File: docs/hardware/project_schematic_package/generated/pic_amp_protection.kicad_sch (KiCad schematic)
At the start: 0 parts

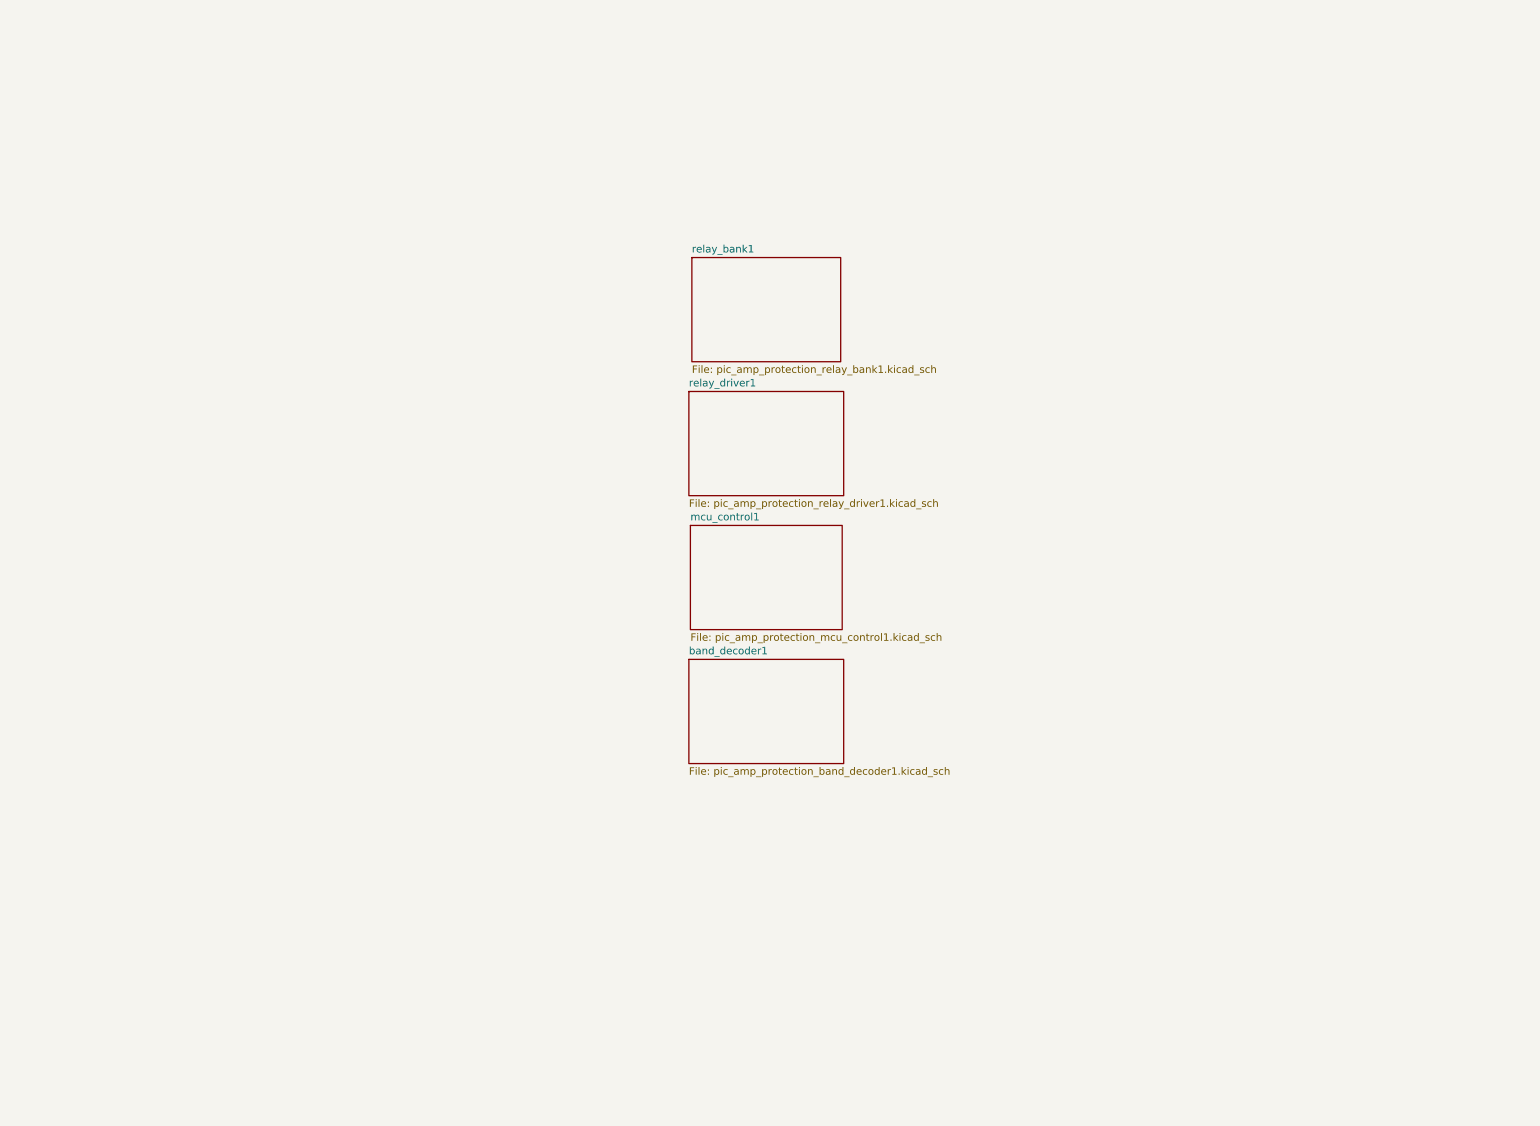
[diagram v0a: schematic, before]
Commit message: Create validated MCP schematic foundation
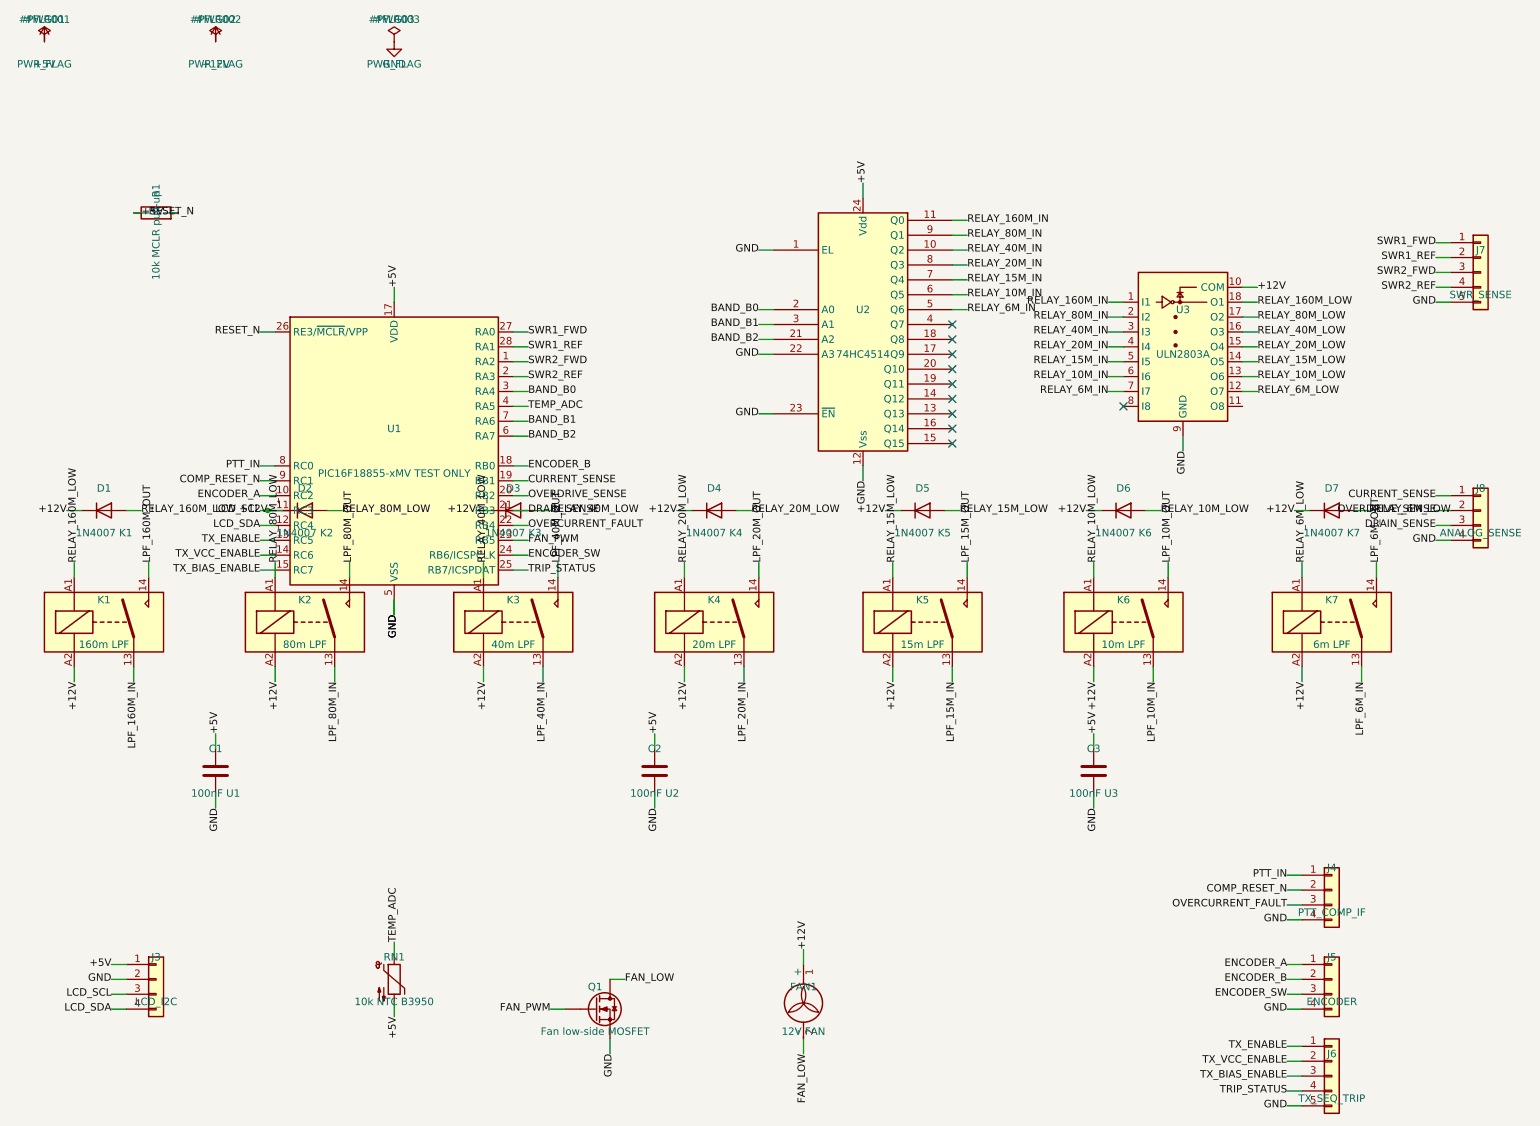
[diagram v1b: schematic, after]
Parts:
- added C1: 100nF U1, symbol Device:C
- added C2: 100nF U2, symbol Device:C
- added C3: 100nF U3, symbol Device:C
- added D1: 1N4007 K1, symbol Device:D
- added D2: 1N4007 K2, symbol Device:D
- added D3: 1N4007 K3, symbol Device:D
- added D4: 1N4007 K4, symbol Device:D
- added D5: 1N4007 K5, symbol Device:D
- added D6: 1N4007 K6, symbol Device:D
- added D7: 1N4007 K7, symbol Device:D
- added FAN1: 12V FAN, symbol Motor:Fan
- added J3: LCD_I2C, symbol Connector_Generic:Conn_01x04
- added J4: PTT_COMP_IF, symbol Connector_Generic:Conn_01x04
- added J5: ENCODER, symbol Connector_Generic:Conn_01x04
- added J6: TX_SEQ_TRIP, symbol Connector_Generic:Conn_01x05
- added J7: SWR_SENSE, symbol Connector_Generic:Conn_01x05
- added J8: ANALOG_SENSE, symbol Connector_Generic:Conn_01x04
- added K1: 160m LPF, symbol Relay:Relay_SPST-NO
- added K2: 80m LPF, symbol Relay:Relay_SPST-NO
- added K3: 40m LPF, symbol Relay:Relay_SPST-NO
- added K4: 20m LPF, symbol Relay:Relay_SPST-NO
- added K5: 15m LPF, symbol Relay:Relay_SPST-NO
- added K6: 10m LPF, symbol Relay:Relay_SPST-NO
- added K7: 6m LPF, symbol Relay:Relay_SPST-NO
- added Q1: Fan low-side MOSFET, symbol Device:Q_NMOS
- added R1: 10k MCLR pull-up, symbol Device:R
- added RN1: 10k NTC B3950, symbol Device:Thermistor_NTC
- added U1: PIC16F18855-xMV TEST ONLY, symbol MCU_Microchip_PIC16:PIC16F18855-xMV
- added U2: 74HC4514, symbol 4xxx_IEEE:4514
- added U3: ULN2803A, symbol Transistor_Array:ULN2803A
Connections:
- new net +12V: D1.1 (K), D2.1 (K), D3.1 (K), D4.1 (K), D5.1 (K), D6.1 (K), D7.1 (K), FAN1.1 (+), J3.3 (Pin_3), K1.A2, K2.A2, K3.A2, K4.A2, K5.A2, K6.A2, K7.A2, U1.11 (RC3), U3.10 (COM)
- new net +5V: C1.1, C2.1, C3.1, J3.1 (Pin_1), R1.2, RN1.2, U1.17 (VDD), U2.24 (Vdd)
- new net BAND_B0: U1.3 (RA4), U2.2 (A0)
- new net BAND_B1: U1.7 (RA6), U2.3 (A1)
- new net BAND_B2: U1.6 (RA7), U2.21 (A2)
- new net COMP_RESET_N: J4.2 (Pin_2), U1.9 (RC1)
- new net CURRENT_SENSE: J8.1 (Pin_1), U1.19 (RB1)
- new net DRAIN_SENSE: J8.3 (Pin_3), U1.21 (RB3)
- new net ENCODER_A: J5.1 (Pin_1), U1.10 (RC2)
- new net ENCODER_B: J5.2 (Pin_2), U1.18 (RB0)
- new net ENCODER_SW: J5.3 (Pin_3), U1.24 (RB6/ICSPCLK)
- new net FAN_LOW: FAN1.2 (-), Q1.D
- new net FAN_PWM: Q1.G, U1.23 (RB5)
- new net GND: C1.2, C2.2, C3.2, J3.2 (Pin_2), J4.4 (Pin_4), J5.4 (Pin_4), J6.5 (Pin_5), J7.5 (Pin_5), J8.4 (Pin_4), Q1.S, U1.16 (VSS), U1.29 (VSS), U1.5 (VSS), U2.1 (EL), U2.12 (Vss), U2.22 (A3), U2.23 (~{EN}), U3.9 (GND)
- new net LCD_SDA: J3.4 (Pin_4), U1.12 (RC4)
- new net LPF_10M_IN: K6.13
- new net LPF_10M_OUT: K6.14
- new net LPF_15M_IN: K5.13
- new net LPF_15M_OUT: K5.14
- new net LPF_160M_IN: K1.13
- new net LPF_160M_OUT: K1.14
- new net LPF_20M_IN: K4.13
- new net LPF_20M_OUT: K4.14
- new net LPF_40M_IN: K3.13
- new net LPF_40M_OUT: K3.14
- new net LPF_6M_IN: K7.13
- new net LPF_6M_OUT: K7.14
- new net LPF_80M_IN: K2.13
- new net LPF_80M_OUT: K2.14
- new net OVERCURRENT_FAULT: J4.3 (Pin_3), U1.22 (RB4)
- new net OVERDRIVE_SENSE: J8.2 (Pin_2), U1.20 (RB2)
- new net PTT_IN: J4.1 (Pin_1), U1.8 (RC0)
- new net RELAY_10M_IN: U2.6 (Q5), U3.6 (I6)
- new net RELAY_10M_LOW: D6.2 (A), K6.A1, U3.13 (O6)
- new net RELAY_15M_IN: U2.7 (Q4), U3.5 (I5)
- new net RELAY_15M_LOW: D5.2 (A), K5.A1, U3.14 (O5)
- new net RELAY_160M_IN: U2.11 (Q0), U3.1 (I1)
- new net RELAY_160M_LOW: D1.2 (A), K1.A1, U3.18 (O1)
- new net RELAY_20M_IN: U2.8 (Q3), U3.4 (I4)
- new net RELAY_20M_LOW: D4.2 (A), K4.A1, U3.15 (O4)
- new net RELAY_40M_IN: U2.10 (Q2), U3.3 (I3)
- new net RELAY_40M_LOW: D3.2 (A), K3.A1, U3.16 (O3)
- new net RELAY_6M_IN: U2.5 (Q6), U3.7 (I7)
- new net RELAY_6M_LOW: D7.2 (A), K7.A1, U3.12 (O7)
- new net RELAY_80M_IN: U2.9 (Q1), U3.2 (I2)
- new net RELAY_80M_LOW: D2.2 (A), K2.A1, U3.17 (O2)
- new net RESET_N: R1.1, U1.26 (RE3/~{MCLR}/VPP)
- new net SWR1_FWD: J7.1 (Pin_1), U1.27 (RA0)
- new net SWR1_REF: J7.2 (Pin_2), U1.28 (RA1)
- new net SWR2_FWD: J7.3 (Pin_3), U1.1 (RA2)
- new net SWR2_REF: J7.4 (Pin_4), U1.2 (RA3)
- new net TEMP_ADC: RN1.1, U1.4 (RA5)
- new net TRIP_STATUS: J6.4 (Pin_4), U1.25 (RB7/ICSPDAT)
- new net TX_BIAS_ENABLE: J6.3 (Pin_3), U1.15 (RC7)
- new net TX_ENABLE: J6.1 (Pin_1), U1.13 (RC5)
- new net TX_VCC_ENABLE: J6.2 (Pin_2), U1.14 (RC6)
- no-connect marks 0 -> 10
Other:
- removed sheet band_decoder1
- removed sheet mcu_control1
- removed sheet relay_bank1
- removed sheet relay_driver1
